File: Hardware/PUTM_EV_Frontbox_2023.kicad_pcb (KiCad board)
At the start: 4 copper layers, 97 x 78 mm, 303 parts, among them IC1 MCP1501T-18E_CHY, IC2 TPS54202HDDCR, J1 Conn_02x16_Counter_Clockwise, J3 M80-5100622, J4 M80-5100622, K1 FINDER-32.21-x000, Q1 NX7002AK, U1 LM4040C33FTA, U10 MCP6001-OT, U11 FODM217B, U12 TLP291-4, U13 TLP291-4, U14 MCP2542FDxMF, U15 MCP6002-xMC, U16 MCP6N11-005, U17 MCP6001, U18 MCP6002-xMC, U19 MCP6N11-005, U2 STM32G473RCTx, U20 MCP6001, U21 MCP6N11-005, U22 MCP6001, U23 MCP6001-OT, U24 AD8226BRMZ-R7, U25 MCP6N11-005, U26 MCP6001, U27 MCP6N11-005, U28 MCP6001, U29 MCP6N11-005, U30 MCP6001, U31 MCP6002-xMC, U32 STLINK-V3MODS, U33 MCP6002-xMC, U34 AD8226BRMZ-R7, U35 AD8226BRMZ-R7, U36 AD8226BRMZ-R7, U37 MCP6001-OT, U4 TLV743P, U6 TLV743P, U7 TLV743P, U8 MCP2542FDxMF, U9 MCP6001-OT, Y1 ABM8G-48.000MHZ

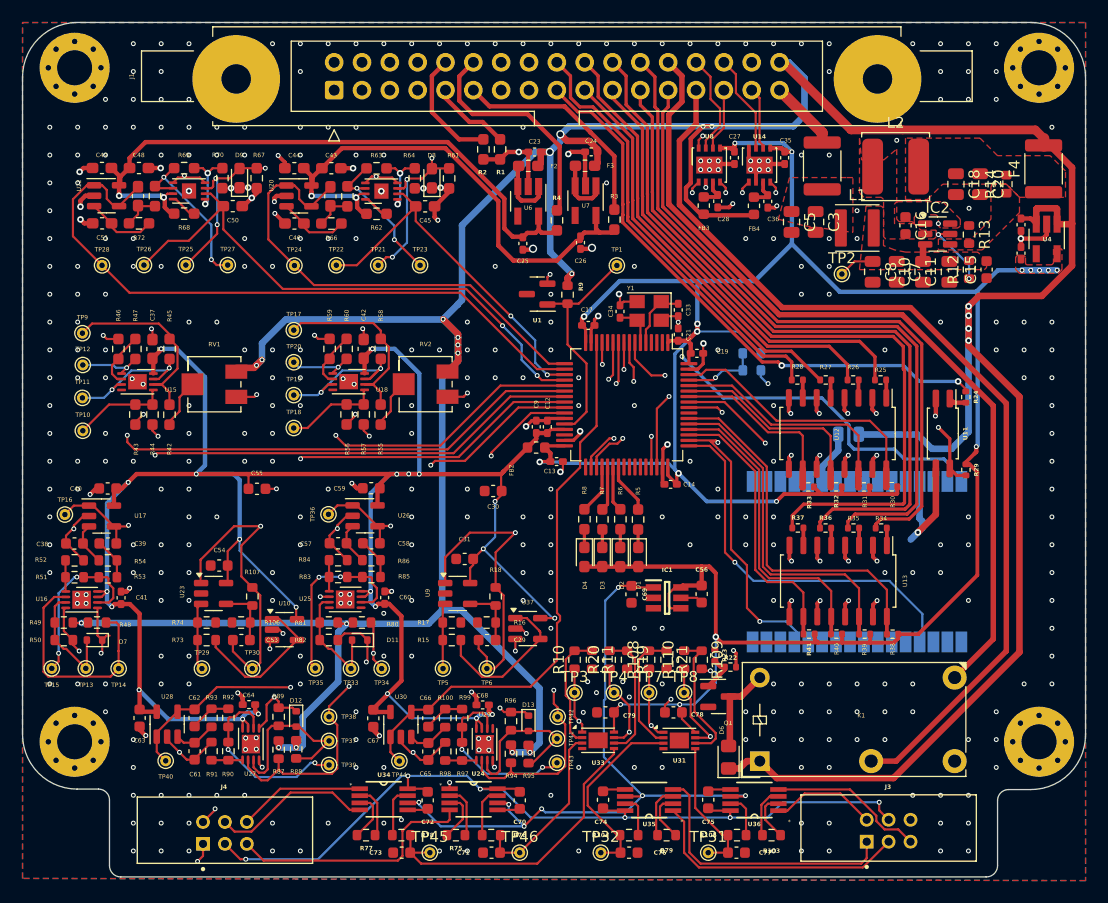
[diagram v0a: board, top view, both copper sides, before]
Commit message: Changes in conventer layout
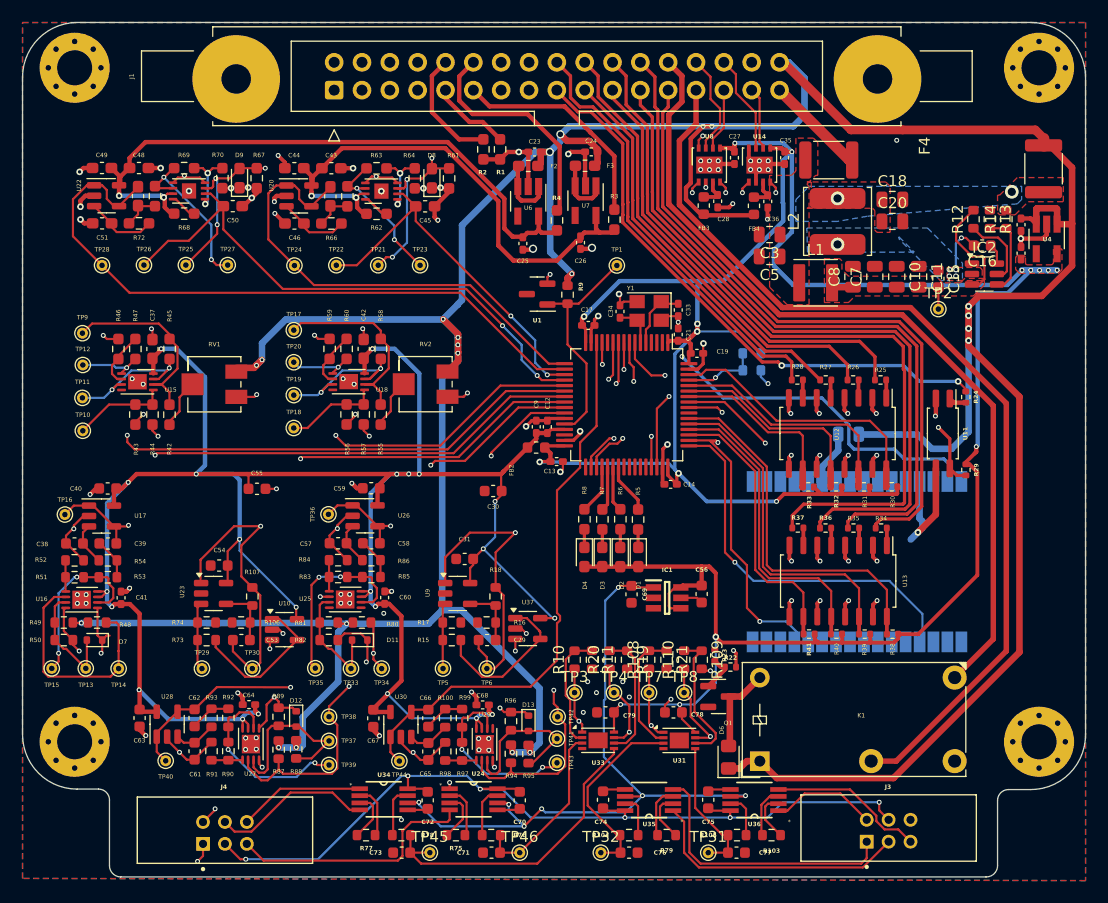
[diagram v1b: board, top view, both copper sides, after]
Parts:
- moved TP2 9.36 mm to (220.0, 91.4)
- moved C20 8.69 mm to (215.8, 83.4), turned to 0 degrees
- moved L2 7.29 mm to (210.8, 83.4), turned to 90 degrees
- moved C16 7.23 mm to (224.0, 85.6), turned to 180 degrees
- moved L1 6.28 mm to (208.8, 89.0)
- moved C18 5.97 mm to (215.8, 81.4), turned to 0 degrees
- moved IC2 5.61 mm to (224.2, 88.2)
- moved R12 4.62 mm to (223.2, 83.2)
- moved C15 4.48 mm to (220.0, 88.6), turned to -90 degrees
- moved C3 4.35 mm to (204.6, 84.6), turned to 180 degrees
- moved C5 3.73 mm to (204.6, 86.6), turned to 180 degrees
- moved R14 3.20 mm to (226.2, 83.2)
- moved C11 2.84 mm to (218.2, 88.5), turned to -90 degrees
- moved C10 2.44 mm to (216.2, 88.5), turned to -90 degrees
- moved R13 2.36 mm to (224.7, 83.2)
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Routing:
- net +3.3V: track 247.4 -> 262.6 mm
- net Net-(IC2-VIN): track 4.91 -> 14.0 mm
- net /Power section/FB_5V: track 0.00 -> 7.88 mm
- net /Power section/SW_5V: track 0.00 -> 4.70 mm, vias 0 -> 6
- net +24V: track 6.39 -> 9.27 mm
- net /Power section/BOOT_5V: track 0.00 -> 1.88 mm
- net /Power section/EN_5V: track 6.28 -> 7.02 mm, vias 2 -> 0
- net GND: track 227.0 -> 227.2 mm, vias 438 -> 128
- net /Power section/5V_UNFUSED: vias 0 -> 2
- added copper zone on B.Cu, net /Power section/5V_UNFUSED
- added copper zone on B.Cu, net /Power section/SW_5V
- removed copper zone on F.Cu, net /Power section/BOOT_5V
- removed copper zone on F.Cu, net /Power section/FB_5V

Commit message: Created hardware version 1.1.0
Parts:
- moved G*** 14.5 mm to (181.0, 110.8)
- moved G*** 7.37 mm to (188.8, 119.1)
- moved J3 0.06 mm to (215.4, 139.0)
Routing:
- net /Power section/5V_UNFUSED: track 0.00 -> 12.7 mm
- net +3.3V: track 262.6 -> 260.0 mm
- net GND: track 227.2 -> 228.6 mm, vias 128 -> 443
- net +5V: track 362.9 -> 363.5 mm
- net /Power section/SW_5V: track 4.70 -> 4.61 mm, vias 6 -> 11
- removed copper zone on B.Cu, net /Power section/5V_UNFUSED

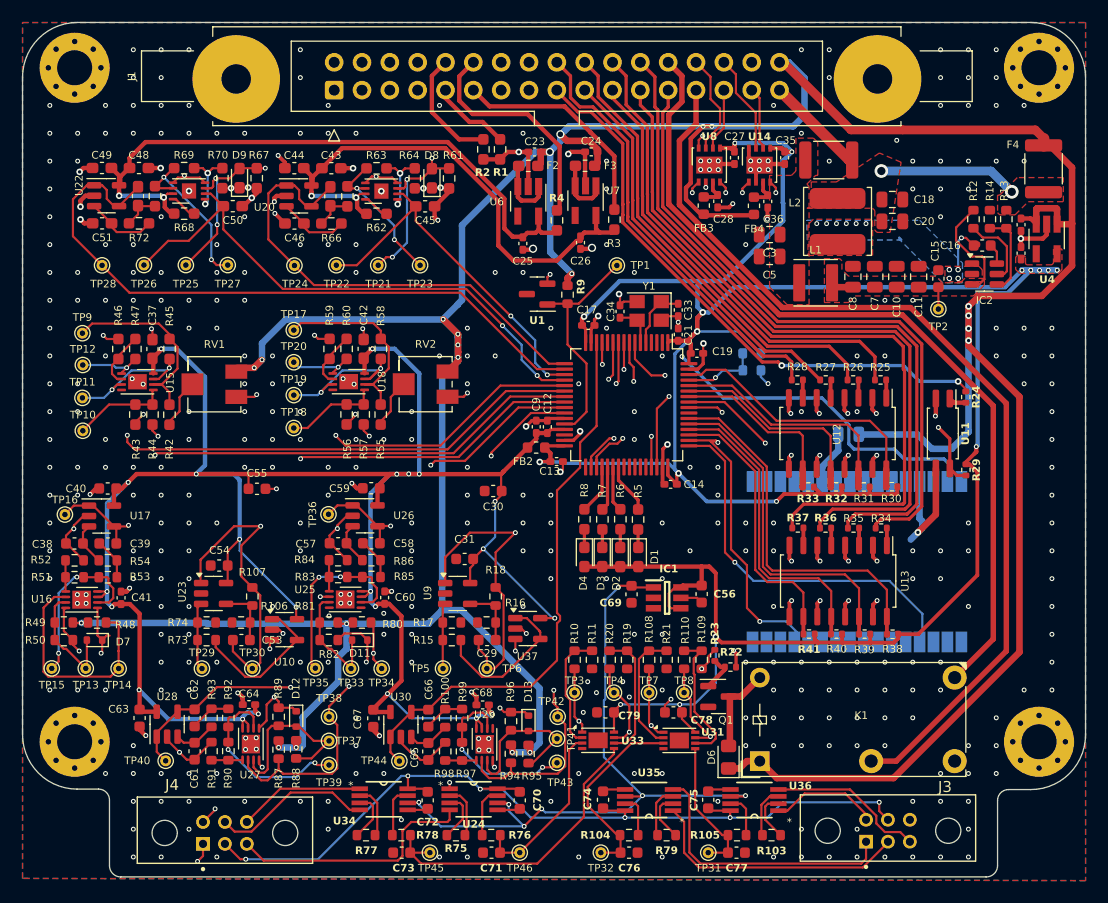
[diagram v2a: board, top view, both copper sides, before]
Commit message: Changes in converter layout and tensometers schematic
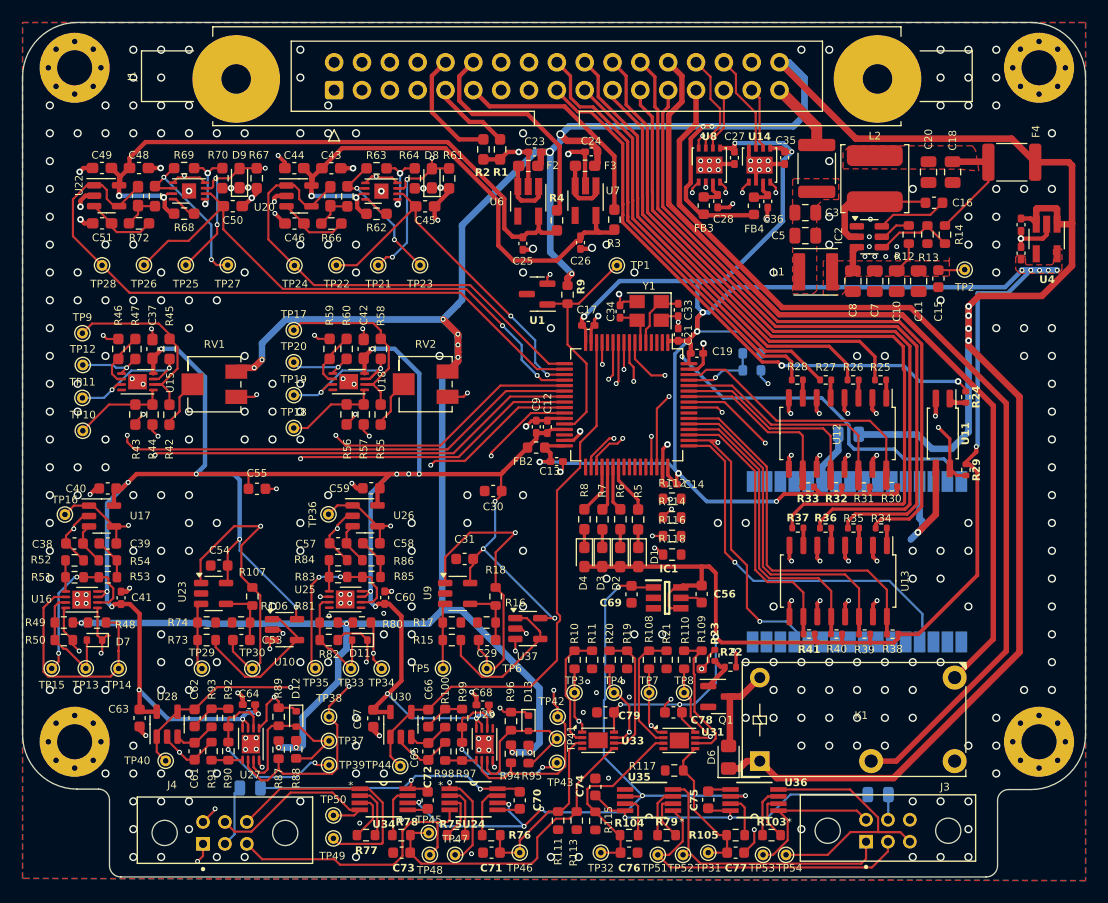
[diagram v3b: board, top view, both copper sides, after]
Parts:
- added F6: 0.5A, Fuse:Fuse_0805_2012Metric, B.Cu at (157.2, 135.1)
- added F7: 0.5A, Fuse:Fuse_0805_2012Metric, B.Cu at (214.5, 135.7)
- added R111: 100K, Resistor_SMD:R_0603_1608Metric, F.Cu at (185.3, 138.1)
- added R112: 100K, Resistor_SMD:R_0603_1608Metric, F.Cu at (195.7, 108.7)
- added R113: 100K, Resistor_SMD:R_0603_1608Metric, F.Cu at (187.0, 138.1)
- added R114: 100K, Resistor_SMD:R_0603_1608Metric, F.Cu at (195.7, 110.4)
- added R115: 100K, Resistor_SMD:R_0603_1608Metric, F.Cu at (188.7, 138.1)
- added R116: 100K, Resistor_SMD:R_0603_1608Metric, F.Cu at (195.7, 112.1)
- added R117: 100K, Resistor_SMD:R_0603_1608Metric, F.Cu at (195.9, 133.5)
- added R118: 100K, Resistor_SMD:R_0603_1608Metric, F.Cu at (195.7, 113.8)
- added TP47: BR_N, TestPoint:TestPoint_THTPad_D1.0mm_Drill0.5mm, F.Cu at (175.9, 141.2)
- added TP48: BR_N, TestPoint:TestPoint_THTPad_D1.0mm_Drill0.5mm, F.Cu at (173.6, 141.2)
- added TP49: BR_N, TestPoint:TestPoint_THTPad_D1.0mm_Drill0.5mm, F.Cu at (164.8, 139.7)
- added TP50: BR_N, TestPoint:TestPoint_THTPad_D1.0mm_Drill0.5mm, F.Cu at (164.8, 137.6)
- added TP51: BR_N, TestPoint:TestPoint_THTPad_D1.0mm_Drill0.5mm, F.Cu at (194.4, 141.2)
- added TP52: BR_N, TestPoint:TestPoint_THTPad_D1.0mm_Drill0.5mm, F.Cu at (196.7, 141.2)
- added TP53: BR_N, TestPoint:TestPoint_THTPad_D1.0mm_Drill0.5mm, F.Cu at (204.0, 141.2)
- added TP54: BR_N, TestPoint:TestPoint_THTPad_D1.0mm_Drill0.5mm, F.Cu at (206.1, 141.2)
- moved IC2 11.0 mm to (213.7, 84.8)
- moved R12 6.06 mm to (217.3, 84.6), turned to -90 degrees
- moved C18 6.04 mm to (221.3, 78.9), turned to -90 degrees
- moved C16 5.88 mm to (219.6, 81.7)
- moved R13 5.87 mm to (219.0, 84.6), turned to 90 degrees
- moved R14 5.77 mm to (220.6, 84.6)
- moved C20 5.58 mm to (219.1, 78.9), turned to -90 degrees
- moved L2 5.17 mm to (214.2, 79.5)
- moved TP2 4.33 mm to (222.4, 87.8)
- moved C3 3.82 mm to (207.9, 82.6)
- moved C5 3.77 mm to (207.9, 84.7)
- moved F4 2.96 mm to (226.7, 78.0), turned to 0 degrees
- moved TP45 1.80 mm to (173.5, 139.2)
- moved C74 1.37 mm to (188.7, 135.0)
- moved F1 1.34 mm to (208.9, 78.6), turned to -90 degrees
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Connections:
- C70 pad 1: +12V -> +12V_LEFT
- C72 pad 1: +12V -> +12V_LEFT
- C74 pad 1: +12V -> +12V_RIGHT
- C75 pad 1: +12V -> +12V_RIGHT
- J3 pad 5: +12V -> /Tensometers/12V2
- J4 pad 2: +12V -> /Tensometers/12V1
- U24 pad 8: +12V -> +12V_LEFT
- U34 pad 8: +12V -> +12V_LEFT
- U35 pad 8: +12V -> +12V_RIGHT
- U36 pad 8: +12V -> +12V_RIGHT
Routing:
- net +12V: track 79.9 -> 0.00 mm, vias 6 -> 0
- net +12V_RIGHT: track 0.00 -> 29.7 mm, vias 0 -> 2
- net +12V_LEFT: track 0.00 -> 27.6 mm, vias 0 -> 2
- net /Tensometers/OUT4+: track 14.4 -> 26.0 mm
- net /Tensometers/OUT2-: track 11.6 -> 22.6 mm
- net /Power section/SW_5V: track 4.61 -> 11.1 mm, vias 11 -> 0
- net /Tensometers/12V1: track 0.00 -> 5.66 mm
- net Net-(IC2-VIN): track 14.0 -> 8.36 mm
- net /Power section/BOOT_5V: track 1.88 -> 6.43 mm
- net /Tensometers/OUT3-: track 24.4 -> 28.9 mm
- net /Tensometers/OUT4-: track 9.94 -> 14.2 mm
- net /Power section/EN_5V: track 7.02 -> 2.89 mm
- net /Tensometers/OUT1-: track 29.1 -> 33.2 mm
- net /Tensometers/OUT1+: track 22.9 -> 26.5 mm
- net +24V: track 9.27 -> 6.41 mm
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- removed copper zone on B.Cu, net /Power section/SW_5V
- removed copper zone on F.Cu, net /Power section/SW_5V
